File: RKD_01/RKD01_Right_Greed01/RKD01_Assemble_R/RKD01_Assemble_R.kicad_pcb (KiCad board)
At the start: 2 copper layers, 197.6 x 126.2 mm, 101 parts, among them J2 TRRS, M1 Mark, M10 Mark, M2 Mark, M3 Mark, M4 Mark, M5 Mark, M6 Mark, M7 Mark, M8 Mark, M9 Mark, SW36 SW_Push, SW37 SW_Push, SW38 SW_Push, SW39 SW_Push, SW40 SW_Push, SW41 SW_Push, SW42 SW_Push, SW43 SW_Push, SW44 SW_Push, SW45 SW_Push, SW46 SW_Push, SW47 SW_Push, SW48 SW_Push, SW49 SW_Push, SW50 SW_Push, SW51 SW_Push, SW52 SW_Push, SW53 SW_Push, SW54 SW_Push, SW55 SW_Push, SW56 SW_Push, SW57 SW_Push, SW58 SW_Push, SW59 SW_Push, SW60 SW_Push, SW61 SW_Push, SW62 SW_Push, SW63 SW_Push, SW64 SW_Push, SW65 SW_Push, SW66 SW_Push, SW67 SW_Push, SW68 SW_Push, SW69 SW_Push, SW70 SW_Push, SW71 SW_Push, SW72 SW_Push, SW73 SW_Push, SW74 SW_Push, SW75 SW_Push, SW76 SW_Push, SW77 SW_Push, SW78 SW_Push, SW79 SW_Push, U2 ProMicro

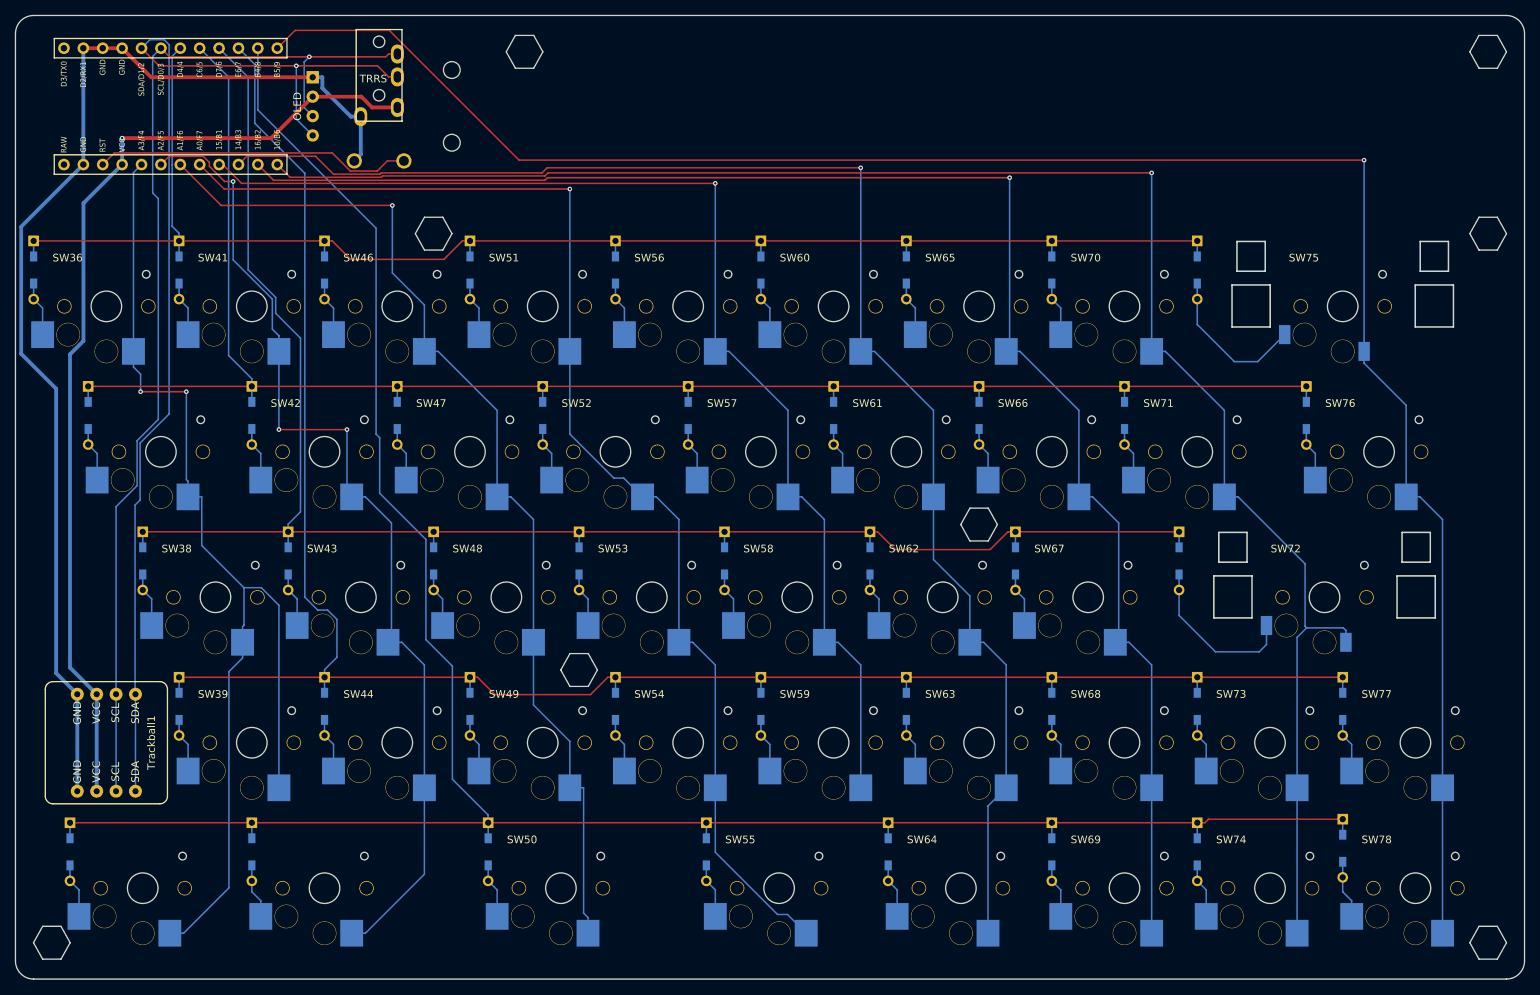
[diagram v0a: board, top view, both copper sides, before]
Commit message: 右配線なおし
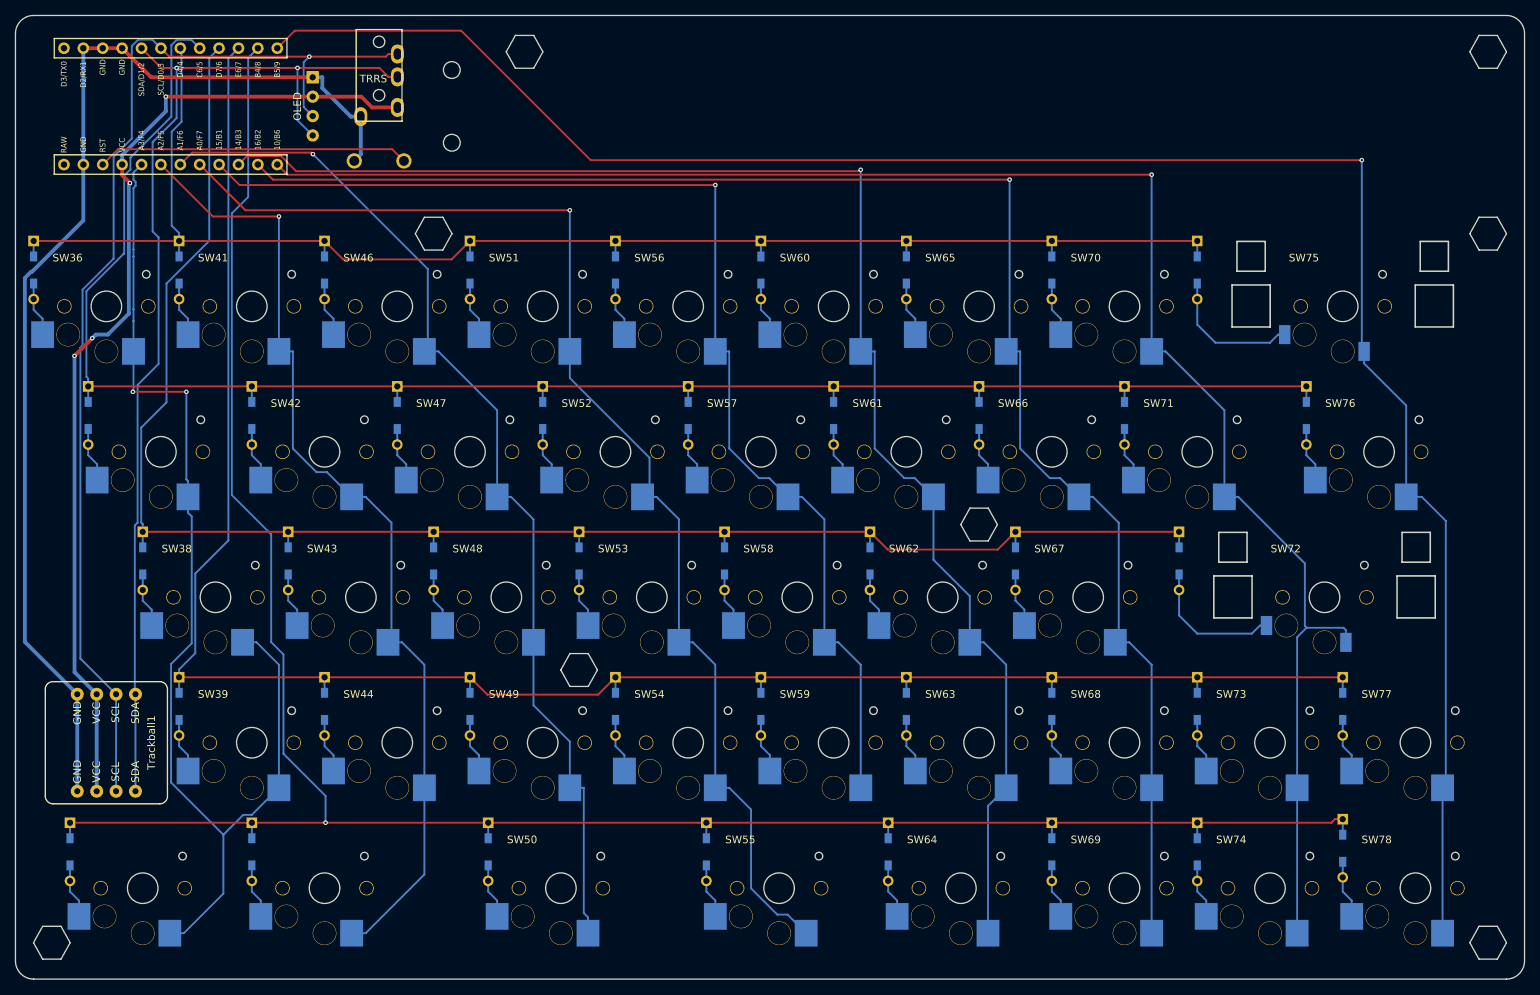
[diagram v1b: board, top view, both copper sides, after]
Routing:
- net Row1: track 225.0 -> 231.7 mm
- net SCL: track 140.5 -> 147.1 mm
- net SDA: track 149.1 -> 142.4 mm, vias 1 -> 2
- net Row4: track 297.1 -> 291.1 mm, vias 0 -> 1
- net Col1: track 133.1 -> 129.3 mm, vias 3 -> 1
- net Row3: track 261.8 -> 258.2 mm
- net Net-(D72-A): track 21.7 -> 18.2 mm
- net Col0: track 146.2 -> 148.5 mm
- net Net-(D75-A): track 20.3 -> 18.2 mm
- net VCC: track 128.7 -> 129.8 mm, vias 1 -> 4
- net Col3: track 163.7 -> 162.8 mm
- net Row2: track 222.4 -> 221.6 mm
- net Col4: track 156.2 -> 156.9 mm
- net Reset: track 41.6 -> 40.9 mm
- net Col2: track 139.1 -> 138.5 mm
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
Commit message: シルクの修正
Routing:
- net Col1: track 129.3 -> 127.4 mm
- net Col4: track 156.9 -> 155.1 mm
- net Col3: track 162.8 -> 161.0 mm
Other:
- board text added: "RKD01_Right_G v1.0"
